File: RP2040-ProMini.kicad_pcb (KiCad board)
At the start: 4 copper layers, 17.8 x 33 mm, 33 parts, among them J1 CONN_L, J2 CONN_U, J3 CONN_R2, J4 CONN_R, Q1 AO3400A, U1 W25Q128JVS, U2 RP2040, U3 MIC5205-3.3YM5, Y1 12MHz

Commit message: Optimized routing even more.
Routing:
- net D10_SS: track 20.9 -> 24.1 mm, vias 2 -> 1
- net D9: track 15.7 -> 13.5 mm
- net D14_A0: track 7.87 -> 6.77 mm
- net +3V3: track 41.7 -> 42.7 mm
- net D2: track 23.2 -> 23.9 mm
- net D11_MOSI: track 14.7 -> 15.4 mm
- net D17_A3: track 12.6 -> 12.0 mm
- net D16_A2: track 10.9 -> 10.3 mm
- net GND: track 27.9 -> 27.8 mm, vias 47 -> 49

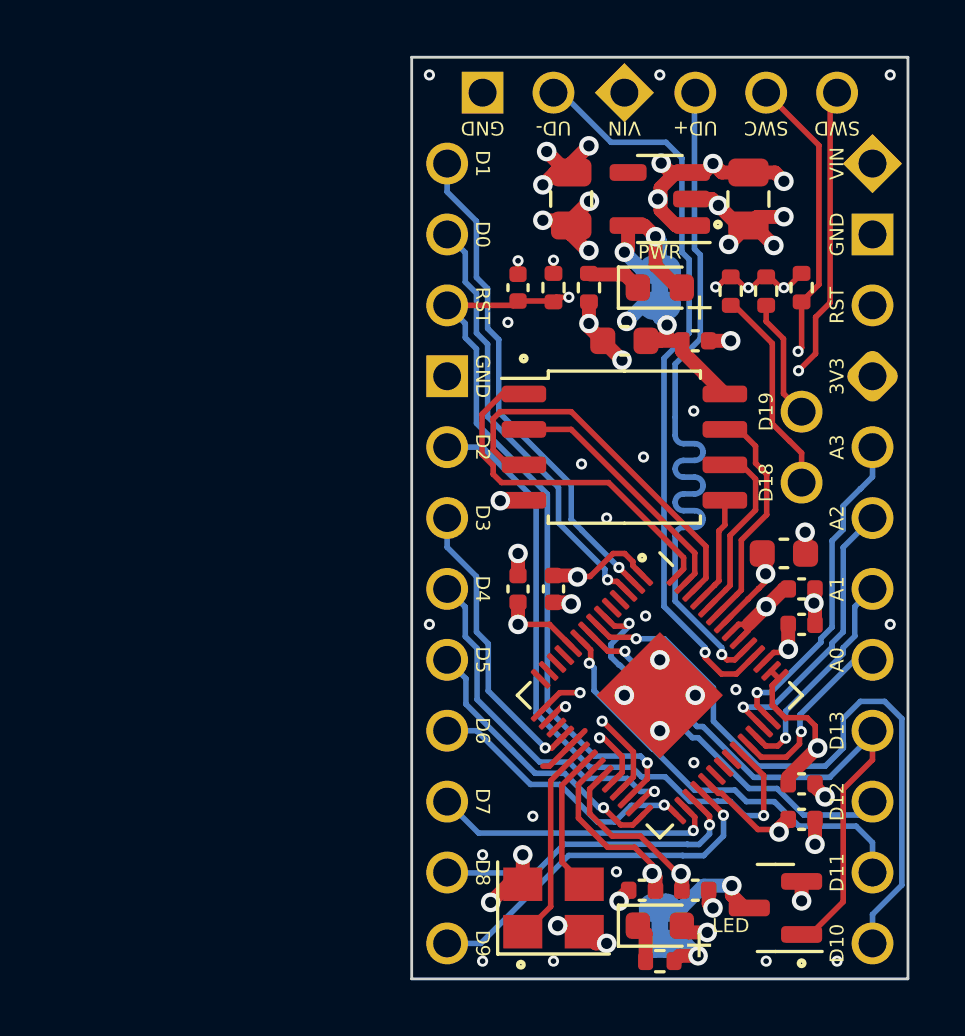
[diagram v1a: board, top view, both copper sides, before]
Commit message: Shaped solder areas for non-gpio pins. Added back silkscreen drawings.
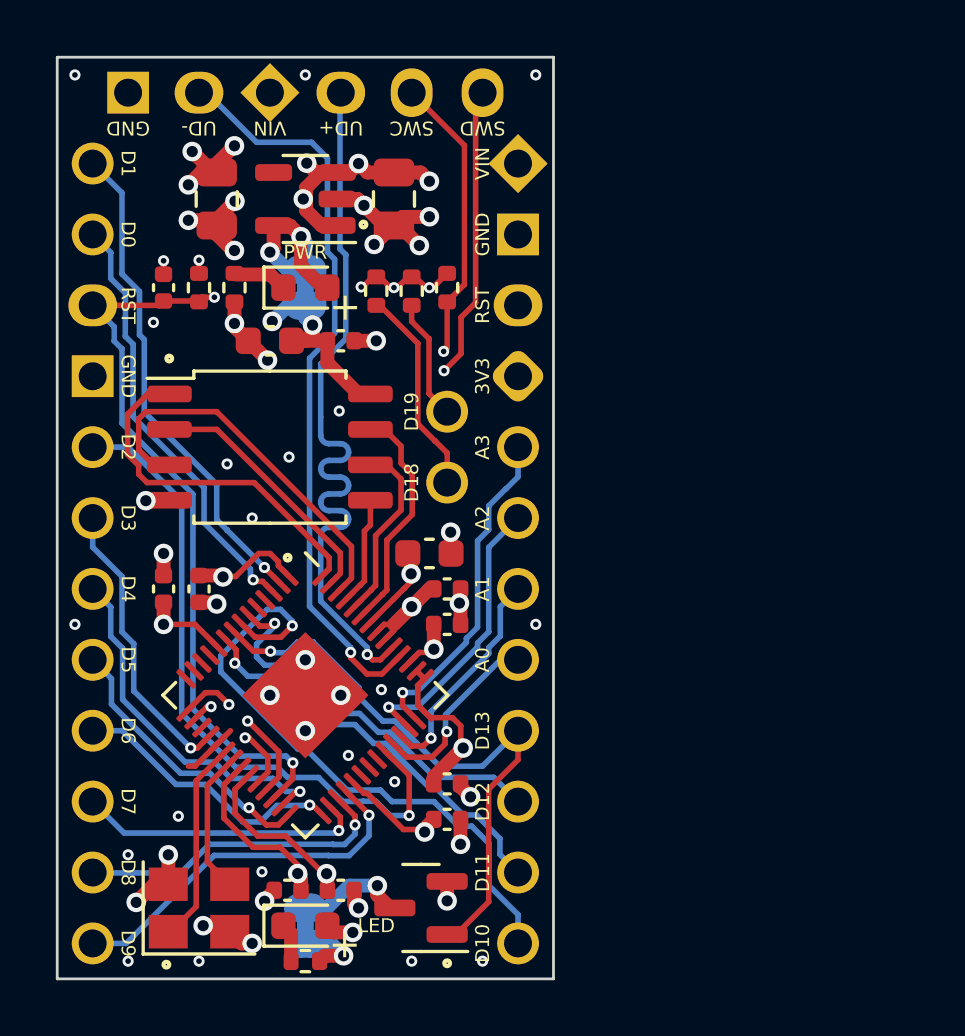
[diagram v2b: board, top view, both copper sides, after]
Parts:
- moved C10 12.7 mm to (139.7, 113.0)
- moved D1 12.7 mm to (143.5, 125.1)
- moved D2 12.7 mm to (143.5, 102.2)
- moved J1 12.7 mm to (135.9, 97.8)
- moved J2 12.7 mm to (137.2, 95.2)
- moved J4 12.7 mm to (151.1, 97.8)
- moved JP1 12.7 mm to (143.5, 125.1)
- moved JP2 12.7 mm to (143.5, 102.2)
- moved R1 12.7 mm to (143.5, 126.4)
- moved R3 12.7 mm to (147.3, 102.4)
- moved R5 12.7 mm to (139.7, 102.2)
- moved U2 12.7 mm to (143.5, 116.8)
- moved U3 12.7 mm to (143.5, 99.1)
- moved Y1 12.7 mm to (139.7, 124.5)
- moved C1 12.7 mm to (142.2, 104.1)
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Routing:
- net D10_SS: track 24.1 -> 22.5 mm
- net D11_MOSI: track 15.4 -> 14.6 mm
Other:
- board text added: "FLASH"
- board text added: "LDO"
- board text added: "MCU"
- board text added: "QRZ"

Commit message: Optimized routing even more.
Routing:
- net SWCLK: track 31.9 -> 32.4 mm
- net GND: vias 49 -> 55

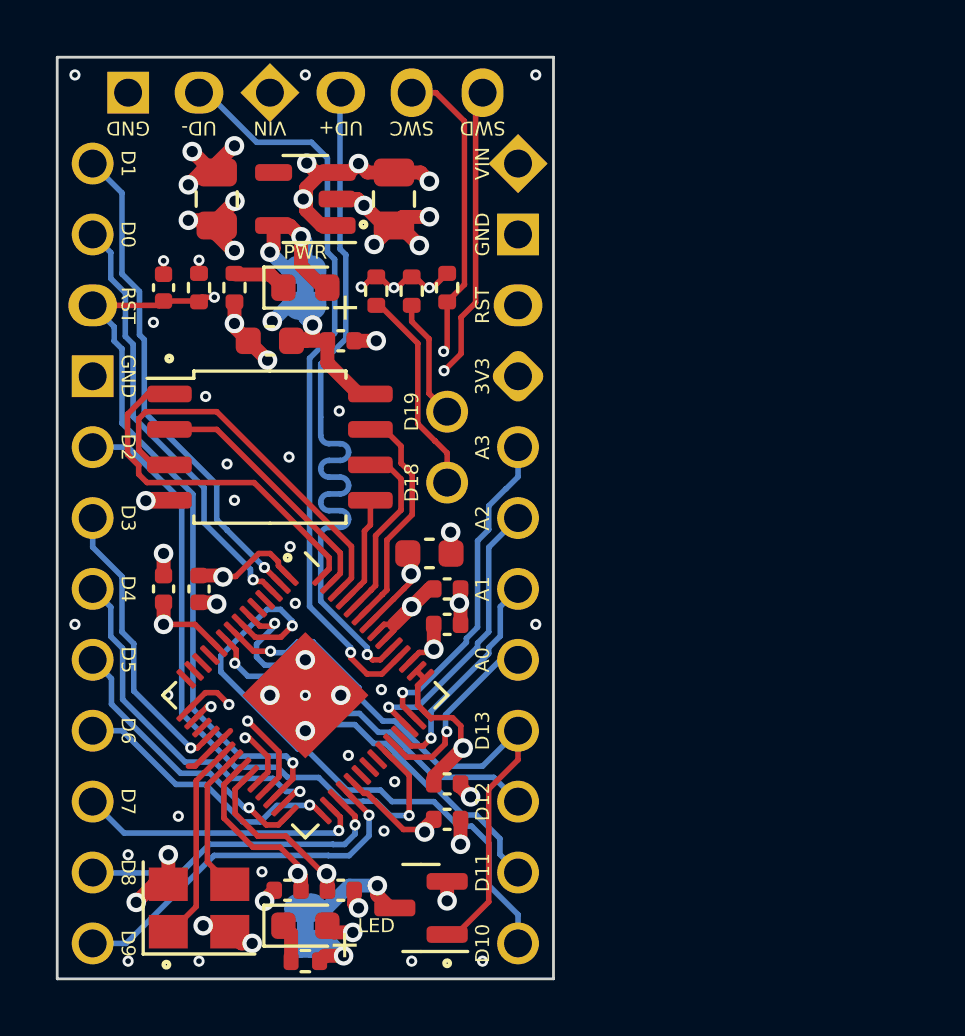
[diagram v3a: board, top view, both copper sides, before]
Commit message: Optimized few traces on PCB. Added few descriptive texts on schematics.
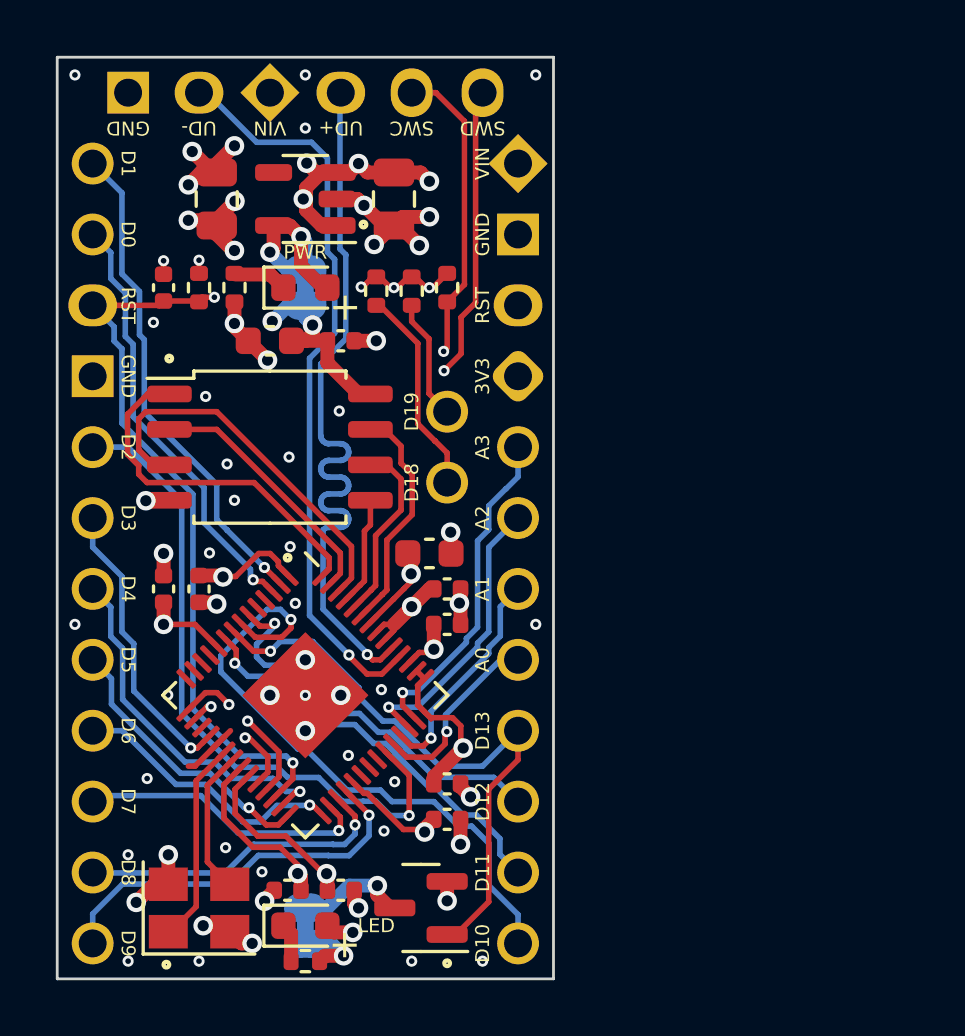
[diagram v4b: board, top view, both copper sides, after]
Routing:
- net D9: track 13.5 -> 14.1 mm
- net GND: vias 55 -> 58

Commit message: Fixed USB trace
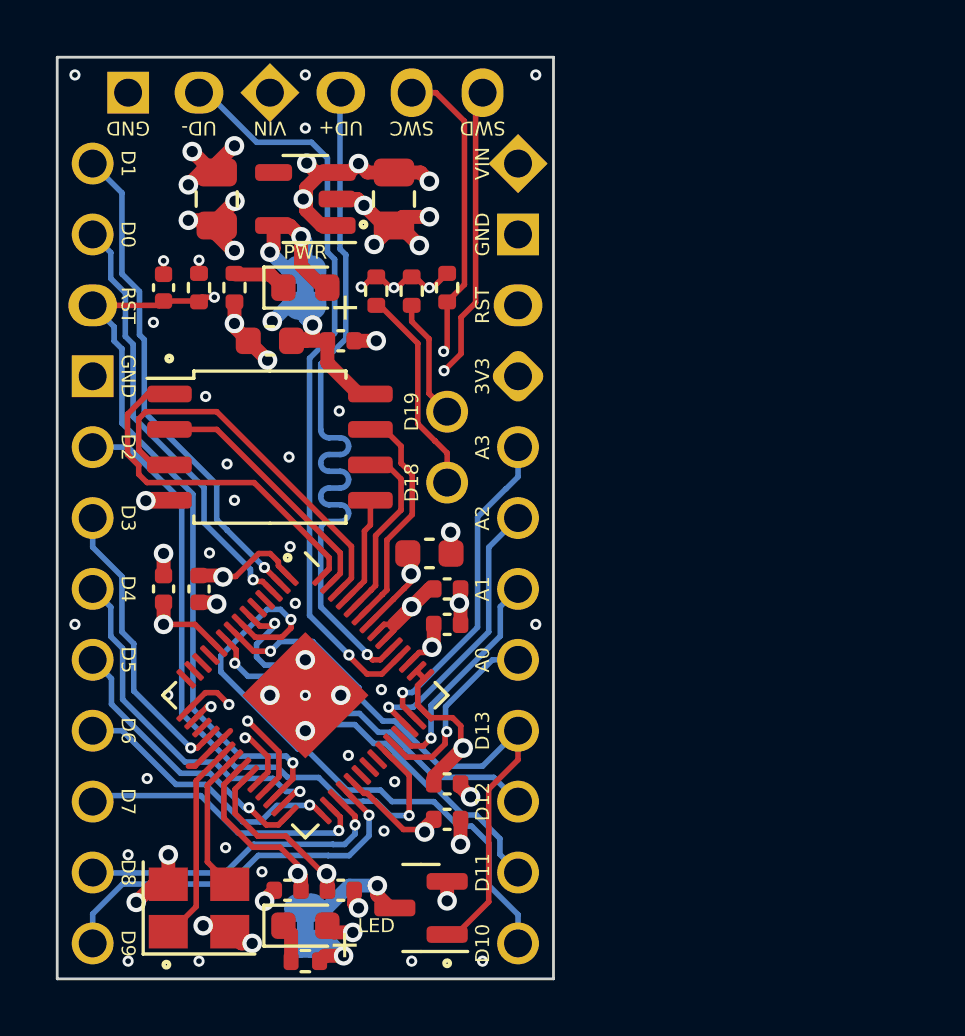
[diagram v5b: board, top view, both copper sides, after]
